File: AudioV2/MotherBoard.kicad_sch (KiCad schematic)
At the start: 62 parts, among them J201 +15/A_GND/-15 out, J202 PD module in (1=GND 2=+12V), Q401 BSS138, Q402 BSS138, SW402 PWR SW, SW501 DEST L (PHONE/MUTE/LINE), SW502 DEST R (PHONE/MUTE/LINE), U201 REC20K-2415DZ, U202 L7809CV +9V, U402 PT2314E, U403 BP5293-50 +5V, U501 OPA1652

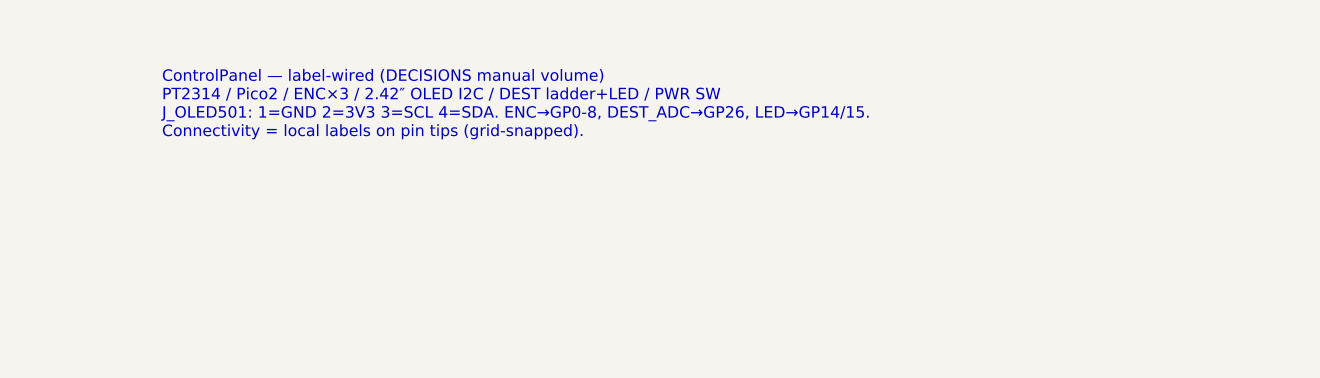
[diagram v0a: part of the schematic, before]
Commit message: AudioV2: ENC_INT に外付けプルアップ、BP5293 注釈を DS に合わせた
MCP23017 の INTA/INTB は OD なので 10k→3V3 を足した。BP5293 の穴は DS
推奨どおり Ø0.9 のまま（「1.2」は外形注記の誤読）で、等ピッチと推奨ランド
を Description に直した。Pico ピン注記と母板の旧 ENC→GP 文も現状へ。

Co-authored-by: m_arino <indare@users.noreply.github.com>
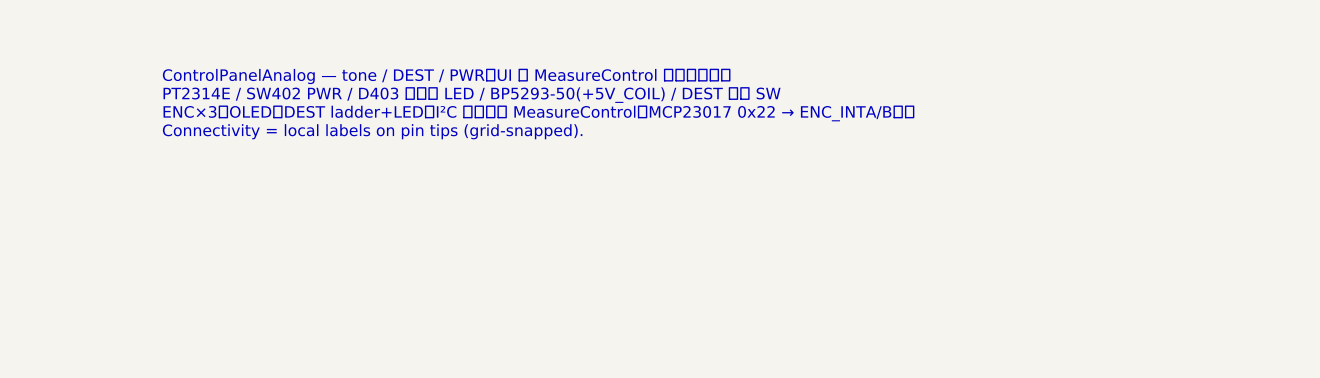
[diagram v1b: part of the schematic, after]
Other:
- note added: "ControlPanelAnalog — tone / DEST / PWR（UI は MeasureControl へ移設済み） PT2314E / SW402 PWR / D403 パネル LED / BP5293-50(+5V_COIL) / DEST 機械 SW ENC×3・OLED・DEST ladder+LED・I²C マスタは MeasureControl（MCP23017 0x22 → ENC_INTA/B）。 Connectivity = local labels on pin tips (grid-snapped)."
- note removed: "ControlPanel — label-wired (DECISIONS manual volume) PT2314 / Pico2 / ENC×3 / 2.42″ OLED I2C / DEST ladder+LED / PWR SW J_OLED501: 1=GND 2=3V3 3=SCL 4=SDA. ENC→GP0-8, DEST_ADC→GP26, LED→GP14/15. Connectivity = local labels on pin tips (grid-snapped)."
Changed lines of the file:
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@@
 		)
 	)
-	(text "ControlPanel — label-wired (DECISIONS manual volume)\nPT2314 / Pico2 / ENC×3 / 2.42″ OLED I2C / DEST ladder+LED / PWR SW\nJ_OLED501: 1=GND 2=3V3 3=SCL 4=SDA. ENC→GP0-8, DEST_ADC→GP26, LED→GP14/15.\nConnectivity = local labels on pin tips (grid-snapped)."
+	(text "ControlPanelAnalog — tone / DEST / PWR（UI は MeasureControl へ移設済み）\nPT2314E / SW402 PWR / D403 パネル LED / BP5293-50(+5V_COIL) / DEST 機械 SW\nENC×3・OLED・DEST ladder+LED・I²C マスタは MeasureControl（MCP23017 0x22 → ENC_INTA/B）。\nConnectivity = local labels on pin tips (grid-snapped)."
 		(exclude_from_sim no)
 		(at 381 25.4 0)
